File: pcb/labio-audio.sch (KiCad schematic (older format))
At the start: 31 parts, among them J701 JACK_TRRS_6PINS, P701 CONN_01X04, P702 CONN_01X04, P703 CONN_01X04, P704 CONN_01X02, SW701 DIP_SWITCH_X04, SW702 DIP_SWITCH_X04, U701 SPU0410HR5H, U702 WM8731

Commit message: combine gnd and gnda nets per mixed signal layout suggestions from analog, ti
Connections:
- net labels removed: GNDA
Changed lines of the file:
@@
-	1    0    0    -1
-$EndComp
-$Comp
-L GNDA #PWR041
-U 1 1 574CC7CB
-P 7000 4200
-F 0 "#PWR041" H 7000 3950 50  0001 C CNN
-F 1 "GNDA" H 7000 4050 50  0000 C CNN
-F 2 "" H 7000 4200 50  0000 C CNN
-F 3 "" H 7000 4200 50  0000 C CNN
-	1    7000 4200
-	1    0    0    -1
-$EndComp
-$Comp
-L GNDA #PWR042
-U 1 1 574CC7ED
-P 7000 1500
-F 0 "#PWR042" H 7000 1250 50  0001 C CNN
-F 1 "GNDA" H 7000 1350 50  0000 C CNN
-F 2 "" H 7000 1500 50  0000 C CNN
-F 3 "" H 7000 1500 50  0000 C CNN
-	1    7000 1500
 	1    0    0    -1
 $EndComp
@@
 Wire Wire Line
 	7300 1000 6900 1000
-$Comp
-L GNDA #PWR044
-U 1 1 574CC826
-P 4300 1600
-F 0 "#PWR044" H 4300 1350 50  0001 C CNN
-F 1 "GNDA" H 4300 1450 50  0000 C CNN
-F 2 "" H 4300 1600 50  0000 C CNN
-F 3 "" H 4300 1600 50  0000 C CNN
-	1    4300 1600
-	1    0    0    -1
-$EndComp
 $Comp
 L GND #PWR045
@@
 Wire Wire Line
 	7000 3900 6900 3900
-$Comp
-L GNDA #PWR046
-U 1 1 574CD08C
-P 7900 5700
-F 0 "#PWR046" H 7900 5450 50  0001 C CNN
-F 1 "GNDA" H 7900 5550 50  0000 C CNN
-F 2 "" H 7900 5700 50  0000 C CNN
-F 3 "" H 7900 5700 50  0000 C CNN
-	1    7900 5700
-	1    0    0    -1
-$EndComp
 Wire Wire Line
 	8100 5800 9000 5800
@@
 	-1   0    0    -1
 $EndComp
-$Comp
-L GNDA #PWR047
-U 1 1 574CE179
-P 3400 4200
-F 0 "#PWR047" H 3400 3950 50  0001 C CNN
-F 1 "GNDA" H 3400 4050 50  0000 C CNN
-F 2 "" H 3400 4200 50  0000 C CNN
-F 3 "" H 3400 4200 50  0000 C CNN
-	1    3400 4200
-	1    0    0    -1
-$EndComp
 Wire Wire Line
 	3400 3400 3400 4200
@@
 	1    3900 5600
 	0    1    1    0
-$EndComp
-$Comp
-L GNDA #PWR048
-U 1 1 574D7F95
-P 3000 6000
-F 0 "#PWR048" H 3000 5750 50  0001 C CNN
-F 1 "GNDA" H 3000 5850 50  0000 C CNN
-F 2 "" H 3000 6000 50  0000 C CNN
-F 3 "" H 3000 6000 50  0000 C CNN
-	1    3000 6000
-	1    0    0    -1
 $EndComp
 $Comp
@@
 	7000 5700 7000 5600
 Connection ~ 7000 5600
-$Comp
-L GNDA #PWR050
-U 1 1 575C906D
-P 6600 6100
-F 0 "#PWR050" H 6600 5850 50  0001 C CNN
-F 1 "GNDA" H 6600 5950 50  0000 C CNN
-F 2 "" H 6600 6100 50  0000 C CNN
-F 3 "" H 6600 6100 50  0000 C CNN
-	1    6600 6100
-	1    0    0    -1
-$EndComp
 Wire Wire Line
 	6600 5900 6600 6100
@@
 	2700 1100 2700 1000
 Connection ~ 2700 1000
+$Comp
+L GND #PWR?
+U 1 1 578E2CA2
+P 7000 1500
+F 0 "#PWR?" H 7000 1250 50  0001 C CNN
+F 1 "GND" H 7000 1350 50  0000 C CNN
+F 2 "" H 7000 1500 50  0000 C CNN
+F 3 "" H 7000 1500 50  0000 C CNN
+	1    7000 1500
+	1    0    0    -1
+$EndComp
+$Comp
+L GND #PWR?
+U 1 1 578E2E7F
+P 4300 1600
+F 0 "#PWR?" H 4300 1350 50  0001 C CNN
+F 1 "GND" H 4300 1450 50  0000 C CNN
+F 2 "" H 4300 1600 50  0000 C CNN
+F 3 "" H 4300 1600 50  0000 C CNN
+	1    4300 1600
+	1    0    0    -1
+$EndComp
+$Comp
+L GND #PWR?
+U 1 1 578E2F07
+P 3400 4200
+F 0 "#PWR?" H 3400 3950 50  0001 C CNN
+F 1 "GND" H 3400 4050 50  0000 C CNN
+F 2 "" H 3400 4200 50  0000 C CNN
+F 3 "" H 3400 4200 50  0000 C CNN
+	1    3400 4200
+	1    0    0    -1
+$EndComp
+$Comp
+L GND #PWR?
+U 1 1 578E300A
+P 3000 6000
+F 0 "#PWR?" H 3000 5750 50  0001 C CNN
+F 1 "GND" H 3000 5850 50  0000 C CNN
+F 2 "" H 3000 6000 50  0000 C CNN
+F 3 "" H 3000 6000 50  0000 C CNN
+	1    3000 6000
+	1    0    0    -1
+$EndComp
+$Comp
+L GND #PWR?
+U 1 1 578E32B4
+P 6600 6100
+F 0 "#PWR?" H 6600 5850 50  0001 C CNN
+F 1 "GND" H 6600 5950 50  0000 C CNN
+F 2 "" H 6600 6100 50  0000 C CNN
+F 3 "" H 6600 6100 50  0000 C CNN
+	1    6600 6100
+	1    0    0    -1
+$EndComp
+$Comp
+L GND #PWR?
+U 1 1 578E335A
+P 7900 5700
+F 0 "#PWR?" H 7900 5450 50  0001 C CNN
+F 1 "GND" H 7900 5550 50  0000 C CNN
+F 2 "" H 7900 5700 50  0000 C CNN
+F 3 "" H 7900 5700 50  0000 C CNN
+	1    7900 5700
+	1    0    0    -1
+$EndComp
+$Comp
+L GND #PWR?
+U 1 1 578E33C2
+P 7000 4200
+F 0 "#PWR?" H 7000 3950 50  0001 C CNN
+F 1 "GND" H 7000 4050 50  0000 C CNN
+F 2 "" H 7000 4200 50  0000 C CNN
+F 3 "" H 7000 4200 50  0000 C CNN
+	1    7000 4200
+	1    0    0    -1
+$EndComp
 $EndSCHEMATC

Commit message: add bom. change led resistors to 220 and dnp rpi hat eeprom
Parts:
- R701: value 2k -> 220
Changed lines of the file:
@@
 P 2700 1500
 F 0 "R701" H 2730 1520 50  0000 L CNN
-F 1 "2k" H 2730 1460 50  0000 L CNN
+F 1 "220" H 2730 1460 50  0000 L CNN
 F 2 "Resistors_SMD:R_0603" H 2700 1500 50  0001 C CNN
 F 3 "" H 2700 1500 50  0000 C CNN

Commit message: Fix board/bom errors from initial build
* Accelerometer (U501) footprint mirrored. Redraw footprint and adjust routing.
* Gyro (U505) footprint mirrored. Redraw footprint and adjust routing.
* Codec (U702) labed as wrong chip. Says WM8731 but should be 8750. Also fix in BOM.
* Should include OLED screen in BOM (not just the connector).
* Codec to TRRS caps have incorrect value. Says 220uF but should be 220pF.
* Mark RPi Hat EEPROM circuit as depopulated in schematic.
* Remove dangling trace near encoder headers.
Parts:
- C714, C715: value 220uF -> 220pF
- U702: value WM8731 -> WM8750; symbol WM8731 -> WM8750
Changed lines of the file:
@@
 $EndDescr
 $Comp
-L WM8731 U702
+L WM8750 U702
 U 1 1 574CC783
 P 6100 2600
 F 0 "U702" H 5500 4400 60  0000 L CNN
-F 1 "WM8731" H 5500 1100 60  0000 L CNN
+F 1 "WM8750" H 5500 1100 60  0000 L CNN
 F 2 "Housings_DFN_QFN:QFN-32-1EP_5x5mm_Pitch0.5mm" H 6100 2600 60  0001 C CNN
 F 3 "" H 6100 2600 60  0000 C CNN
@@
 Connection ~ 7000 1400
 $Comp
-L GND #PWR041
+L GND #PWR710
 U 1 1 574CC80B
 P 7300 1500
-F 0 "#PWR041" H 7300 1250 50  0001 C CNN
+F 0 "#PWR710" H 7300 1250 50  0001 C CNN
 F 1 "GND" H 7300 1350 50  0000 C CNN
 F 2 "" H 7300 1500 50  0000 C CNN
@@
 	7300 1000 6900 1000
 $Comp
-L GND #PWR042
+L GND #PWR703
 U 1 1 574CC834
 P 3400 1600
-F 0 "#PWR042" H 3400 1350 50  0001 C CNN
+F 0 "#PWR703" H 3400 1350 50  0001 C CNN
 F 1 "GND" H 3400 1450 50  0000 C CNN
 F 2 "" H 3400 1600 50  0000 C CNN
@@
 P 8000 2900
 F 0 "C715" H 8010 2970 50  0000 L CNN
-F 1 "220uF" H 8010 2820 50  0000 L CNN
+F 1 "220pF" H 8010 2820 50  0000 L CNN
 F 2 "Capacitors_SMD:C_0603" H 8000 2900 50  0001 C CNN
 F 3 "" H 8000 2900 50  0000 C CNN
@@
 P 8000 2500
 F 0 "C714" H 8010 2570 50  0000 L CNN
-F 1 "220uF" H 8010 2420 50  0000 L CNN
+F 1 "220pF" H 8010 2420 50  0000 L CNN
 F 2 "Capacitors_SMD:C_0603" H 8000 2500 50  0001 C CNN
 F 3 "" H 8000 2500 50  0000 C CNN
@@
 	4800 2500 5300 2500
 $Comp
-L GND #PWR043
+L GND #PWR706
 U 1 1 574D9E5B
 P 5000 2800
-F 0 "#PWR043" H 5000 2550 50  0001 C CNN
+F 0 "#PWR706" H 5000 2550 50  0001 C CNN
 F 1 "GND" H 5000 2650 50  0000 C CNN
 F 2 "" H 5000 2800 50  0000 C CNN
@@
 $EndComp
 $Comp
-L GND #PWR044
+L GND #PWR701
 U 1 1 576D6E7D
 P 2700 1700
-F 0 "#PWR044" H 2700 1450 50  0001 C CNN
+F 0 "#PWR701" H 2700 1450 50  0001 C CNN
 F 1 "GND" H 2700 1550 50  0000 C CNN
 F 2 "" H 2700 1700 50  0000 C CNN
@@
 Connection ~ 2700 1000
 $Comp
-L GND #PWR045
+L GND #PWR708
 U 1 1 578E2CA2
 P 7000 1500
-F 0 "#PWR045" H 7000 1250 50  0001 C CNN
+F 0 "#PWR708" H 7000 1250 50  0001 C CNN
 F 1 "GND" H 7000 1350 50  0000 C CNN
 F 2 "" H 7000 1500 50  0000 C CNN
@@
 $EndComp
 $Comp
-L GND #PWR046
+L GND #PWR705
 U 1 1 578E2E7F
 P 4300 1600
-F 0 "#PWR046" H 4300 1350 50  0001 C CNN
+F 0 "#PWR705" H 4300 1350 50  0001 C CNN
 F 1 "GND" H 4300 1450 50  0000 C CNN
 F 2 "" H 4300 1600 50  0000 C CNN
@@
 $EndComp
 $Comp
-L GND #PWR047
+L GND #PWR704
 U 1 1 578E2F07
 P 3400 4200
-F 0 "#PWR047" H 3400 3950 50  0001 C CNN
+F 0 "#PWR704" H 3400 3950 50  0001 C CNN
 F 1 "GND" H 3400 4050 50  0000 C CNN
 F 2 "" H 3400 4200 50  0000 C CNN
@@
 $EndComp
 $Comp
-L GND #PWR048
+L GND #PWR702
 U 1 1 578E300A
 P 3000 6000
-F 0 "#PWR048" H 3000 5750 50  0001 C CNN
+F 0 "#PWR702" H 3000 5750 50  0001 C CNN
 F 1 "GND" H 3000 5850 50  0000 C CNN
 F 2 "" H 3000 6000 50  0000 C CNN
@@
 $EndComp
 $Comp
-L GND #PWR049
+L GND #PWR707
 U 1 1 578E32B4
 P 6600 6100
-F 0 "#PWR049" H 6600 5850 50  0001 C CNN
+F 0 "#PWR707" H 6600 5850 50  0001 C CNN
 F 1 "GND" H 6600 5950 50  0000 C CNN
 F 2 "" H 6600 6100 50  0000 C CNN
@@
 $EndComp
 $Comp
-L GND #PWR050
+L GND #PWR711
 U 1 1 578E335A
 P 7900 5700
-F 0 "#PWR050" H 7900 5450 50  0001 C CNN
+F 0 "#PWR711" H 7900 5450 50  0001 C CNN
 F 1 "GND" H 7900 5550 50  0000 C CNN
 F 2 "" H 7900 5700 50  0000 C CNN
@@
 $EndComp
 $Comp
-L GND #PWR051
+L GND #PWR709
 U 1 1 578E33C2
 P 7000 4200
-F 0 "#PWR051" H 7000 3950 50  0001 C CNN
+F 0 "#PWR709" H 7000 3950 50  0001 C CNN
 F 1 "GND" H 7000 4050 50  0000 C CNN
 F 2 "" H 7000 4200 50  0000 C CNN

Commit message: Use soldermask windows on footprints with thermal pads (motor driver, codec)
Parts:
- U702: footprint Housings_DFN_QFN:QFN-32-1EP_5x5mm_Pitch0.5mm -> labio-special:QFN-32-1EP_5x5mm_Pitch0.5mm
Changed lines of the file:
@@
 F 0 "U702" H 5500 4400 60  0000 L CNN
 F 1 "WM8750" H 5500 1100 60  0000 L CNN
-F 2 "Housings_DFN_QFN:QFN-32-1EP_5x5mm_Pitch0.5mm" H 6100 2600 60  0001 C CNN
+F 2 "labio-special:QFN-32-1EP_5x5mm_Pitch0.5mm" H 6100 2600 60  0001 C CNN
 F 3 "" H 6100 2600 60  0000 C CNN
 	1    6100 2600
@@
 Connection ~ 7000 1400
 $Comp
-L GND #PWR710
+L GND #PWR041
 U 1 1 574CC80B
 P 7300 1500
-F 0 "#PWR710" H 7300 1250 50  0001 C CNN
+F 0 "#PWR041" H 7300 1250 50  0001 C CNN
 F 1 "GND" H 7300 1350 50  0000 C CNN
 F 2 "" H 7300 1500 50  0000 C CNN
@@
 	7300 1000 6900 1000
 $Comp
-L GND #PWR703
+L GND #PWR042
 U 1 1 574CC834
 P 3400 1600
-F 0 "#PWR703" H 3400 1350 50  0001 C CNN
+F 0 "#PWR042" H 3400 1350 50  0001 C CNN
 F 1 "GND" H 3400 1450 50  0000 C CNN
 F 2 "" H 3400 1600 50  0000 C CNN
@@
 	4800 2500 5300 2500
 $Comp
-L GND #PWR706
+L GND #PWR043
 U 1 1 574D9E5B
 P 5000 2800
-F 0 "#PWR706" H 5000 2550 50  0001 C CNN
+F 0 "#PWR043" H 5000 2550 50  0001 C CNN
 F 1 "GND" H 5000 2650 50  0000 C CNN
 F 2 "" H 5000 2800 50  0000 C CNN
@@
 $EndComp
 $Comp
-L GND #PWR701
+L GND #PWR044
 U 1 1 576D6E7D
 P 2700 1700
-F 0 "#PWR701" H 2700 1450 50  0001 C CNN
+F 0 "#PWR044" H 2700 1450 50  0001 C CNN
 F 1 "GND" H 2700 1550 50  0000 C CNN
 F 2 "" H 2700 1700 50  0000 C CNN
@@
 Connection ~ 2700 1000
 $Comp
-L GND #PWR708
+L GND #PWR045
 U 1 1 578E2CA2
 P 7000 1500
-F 0 "#PWR708" H 7000 1250 50  0001 C CNN
+F 0 "#PWR045" H 7000 1250 50  0001 C CNN
 F 1 "GND" H 7000 1350 50  0000 C CNN
 F 2 "" H 7000 1500 50  0000 C CNN
@@
 $EndComp
 $Comp
-L GND #PWR705
+L GND #PWR046
 U 1 1 578E2E7F
 P 4300 1600
-F 0 "#PWR705" H 4300 1350 50  0001 C CNN
+F 0 "#PWR046" H 4300 1350 50  0001 C CNN
 F 1 "GND" H 4300 1450 50  0000 C CNN
 F 2 "" H 4300 1600 50  0000 C CNN
@@
 $EndComp
 $Comp
-L GND #PWR704
+L GND #PWR047
 U 1 1 578E2F07
 P 3400 4200
-F 0 "#PWR704" H 3400 3950 50  0001 C CNN
+F 0 "#PWR047" H 3400 3950 50  0001 C CNN
 F 1 "GND" H 3400 4050 50  0000 C CNN
 F 2 "" H 3400 4200 50  0000 C CNN
@@
 $EndComp
 $Comp
-L GND #PWR702
+L GND #PWR048
 U 1 1 578E300A
 P 3000 6000
-F 0 "#PWR702" H 3000 5750 50  0001 C CNN
+F 0 "#PWR048" H 3000 5750 50  0001 C CNN
 F 1 "GND" H 3000 5850 50  0000 C CNN
 F 2 "" H 3000 6000 50  0000 C CNN
@@
 $EndComp
 $Comp
-L GND #PWR707
+L GND #PWR049
 U 1 1 578E32B4
 P 6600 6100
-F 0 "#PWR707" H 6600 5850 50  0001 C CNN
+F 0 "#PWR049" H 6600 5850 50  0001 C CNN
 F 1 "GND" H 6600 5950 50  0000 C CNN
 F 2 "" H 6600 6100 50  0000 C CNN
@@
 $EndComp
 $Comp
-L GND #PWR711
+L GND #PWR050
 U 1 1 578E335A
 P 7900 5700
-F 0 "#PWR711" H 7900 5450 50  0001 C CNN
+F 0 "#PWR050" H 7900 5450 50  0001 C CNN
 F 1 "GND" H 7900 5550 50  0000 C CNN
 F 2 "" H 7900 5700 50  0000 C CNN
@@
 $EndComp
 $Comp
-L GND #PWR709
+L GND #PWR051
 U 1 1 578E33C2
 P 7000 4200
-F 0 "#PWR709" H 7000 3950 50  0001 C CNN
+F 0 "#PWR051" H 7000 3950 50  0001 C CNN
 F 1 "GND" H 7000 4050 50  0000 C CNN
 F 2 "" H 7000 4200 50  0000 C CNN

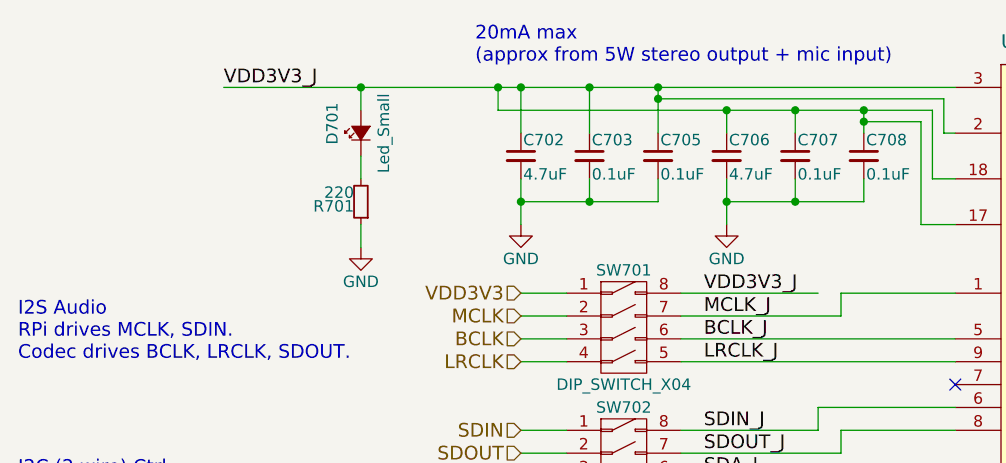
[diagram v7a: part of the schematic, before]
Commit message: add fuses for connectable headers (adc, encoder, motors, servo, codec). GERBER/BOM UPDATES ONLY
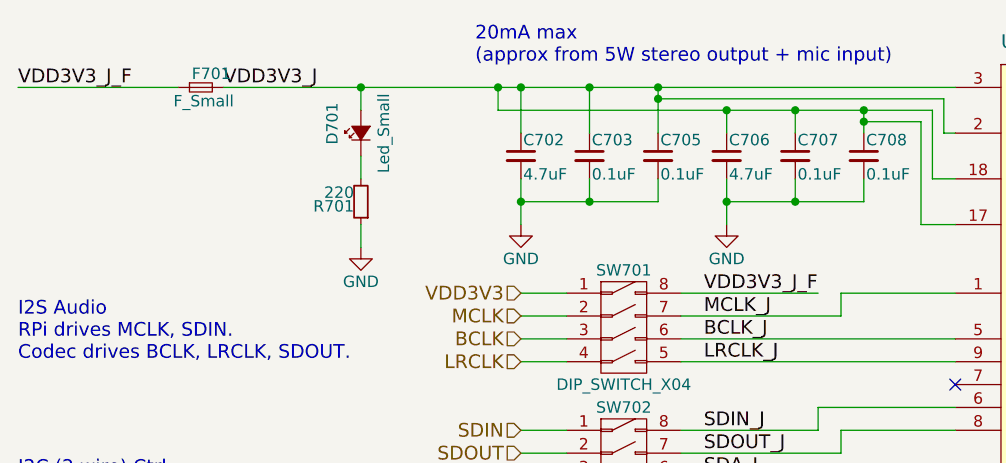
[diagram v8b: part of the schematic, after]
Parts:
- added F701: F_Small, Resistors_SMD:R_1206, symbol F_Small
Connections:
- net VDD3V3_J: now also F701.2; no longer SW701.8 (1B)
- new net VDD3V3_J_F: F701.1, SW701.8 (1B)
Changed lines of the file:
@@
 	4100 1900 4700 1900
 Text Label 4200 1900 0    60   ~ 0
-VDD3V3_J
+VDD3V3_J_F
 Wire Wire Line
 	3600 1900 3400 1900
@@
 	1    0    0    -1
 $EndComp
+$Comp
+L F_Small F701
+U 1 1 57A581AC
+P 2000 1000
+F 0 "F701" H 1960 1060 50  0000 L CNN
+F 1 "F_Small" H 1880 940 50  0000 L CNN
+F 2 "Resistors_SMD:R_1206" H 2000 1000 50  0001 C CNN
+F 3 "" H 2000 1000 50  0000 C CNN
+	1    2000 1000
+	1    0    0    -1
+$EndComp
+Wire Wire Line
+	1900 1000 1200 1000
+Text Label 1200 1000 0    60   ~ 0
+VDD3V3_J_F
 $EndSCHEMATC
